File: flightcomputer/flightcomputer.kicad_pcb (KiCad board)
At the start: 4 copper layers, 100 x 75 mm, 63 parts, among them J1 Conn_Coaxial, J10 Conn_01x03, J11 Conn_01x03, J12 ESQ-113-14-G-D, J14 S3B-PH-K-S-GW, J2 Conn_Coaxial, J3 Conn_Coaxial, J4 Conn_Coaxial, J5 S3B-PH-K-S-GW, J6 Conn_01x03, J7 S4B-PH-K-S_LF__SN_, J8 Conn_01x03, J9 Conn_01x06, U1 MAX-M10S, U2 LIS2MDLTR, U3 BMI088, U4 MS5607-02BA, U7 Teensy4.1, U8 LSM6DSO32TR, U9 RFM96W-433S2

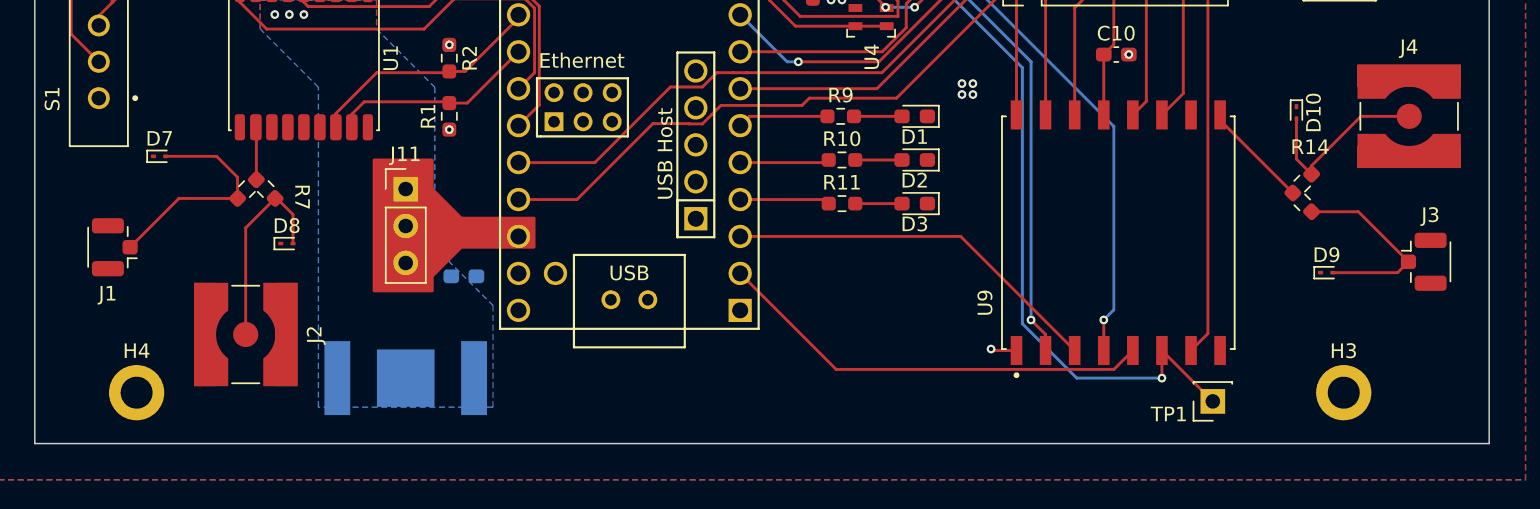
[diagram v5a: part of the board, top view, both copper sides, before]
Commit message: killed BMS, updated pyro fets with lower resistance, updated inductor, replace + reroute, fixed some DRC in flight computer (dont know why remaining are being caused, hopefully jlc doesnt care), next todo is to kill myself
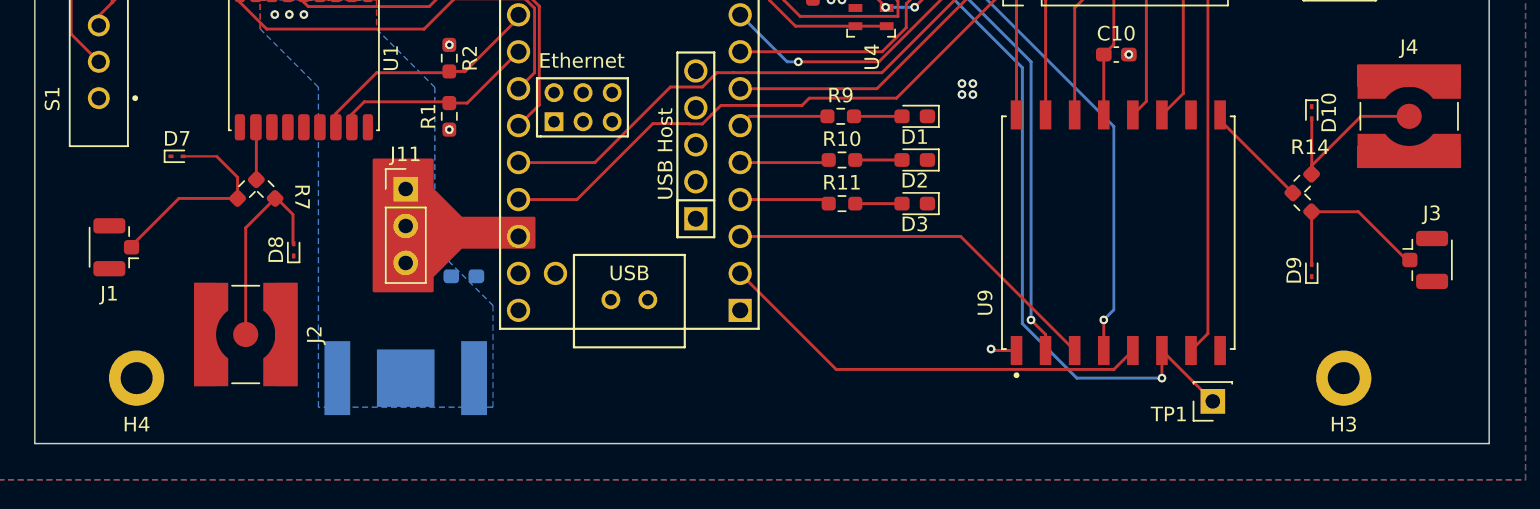
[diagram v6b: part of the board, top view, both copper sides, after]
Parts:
- moved D7 1.20 mm to (44.8, 117.8)
- moved D10 1.05 mm to (122.8, 114.8)
- moved D9 1.04 mm to (122.8, 125.6), turned to 90 degrees
- moved H3 1.00 mm to (125.0, 133.0)
- moved H4 1.00 mm to (42.0, 133.0)
- moved D8 0.64 mm to (52.8, 124.2), turned to 90 degrees
- moved J3 0.16 mm to (130.6, 124.9)
- moved J1 0.10 mm to (40.6, 124.0)
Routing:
- net Net-(D9-A2): track 13.6 -> 11.7 mm
- net Net-(D7-A2): track 15.8 -> 14.6 mm
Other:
- rule pad_to_mask_clearance: 0.1 -> 0.05

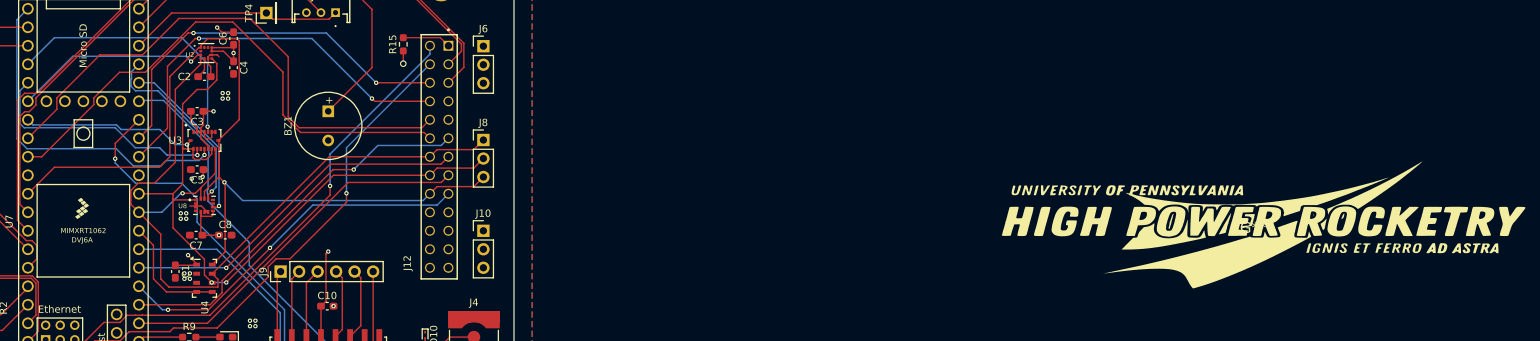
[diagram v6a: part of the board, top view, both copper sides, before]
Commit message: fixed fc silkscreen drc + added hpr logo, coax violation seems intentional so can be ignored, jlc says tolerance 0.127 so 0.13mm should be fine
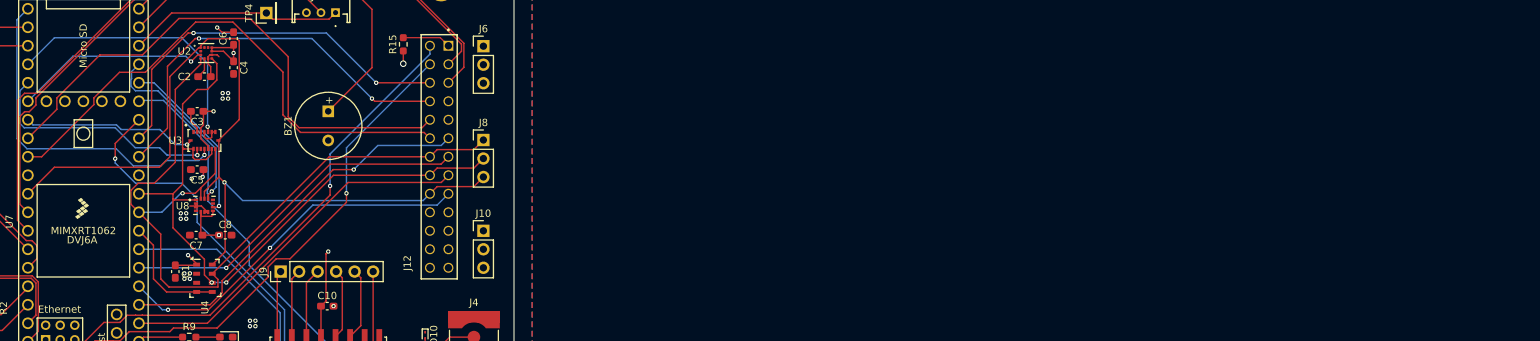
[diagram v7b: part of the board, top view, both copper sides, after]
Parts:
- G***: moved to B.Cu
- moved G*** 142.2 mm to (94.8, 101.4), turned to 90 degrees
